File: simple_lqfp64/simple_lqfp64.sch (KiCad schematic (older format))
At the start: 47 parts, among them P1 CONN_01X02, P10 CONN_01X04, P11 CONN_01X03, P12 CONN_01X03, P13 USB_A, P14 CONN_01X01, P15 CONN_01X01, P16 CONN_01X01, P17 CONN_01X01, P18 CONN_01X01, P19 CONN_01X01, P2 CONN_01X03, P20 CONN_01X01, P21 CONN_01X01, P22 CONN_01X01, P23 CONN_01X01, P24 CONN_01X01, P25 CONN_01X01, P26 CONN_01X01, P27 CONN_01X01, P28 CONN_01X01, P29 CONN_01X01, P3 CONN_01X04, P30 CONN_01X01, P31 CONN_01X01, P32 CONN_01X01, P33 CONN_01X01, P4 CONN_01X04, P5 CONN_01X01, P6 CONN_01X04, P7 CONN_01X03, P8 CONN_01X06, P9 CONN_01X07, SW1 SW_PUSH, U1 STM32F103RCTx, U2 AP1117D33, Y1 Crystal, Y2 Crystal

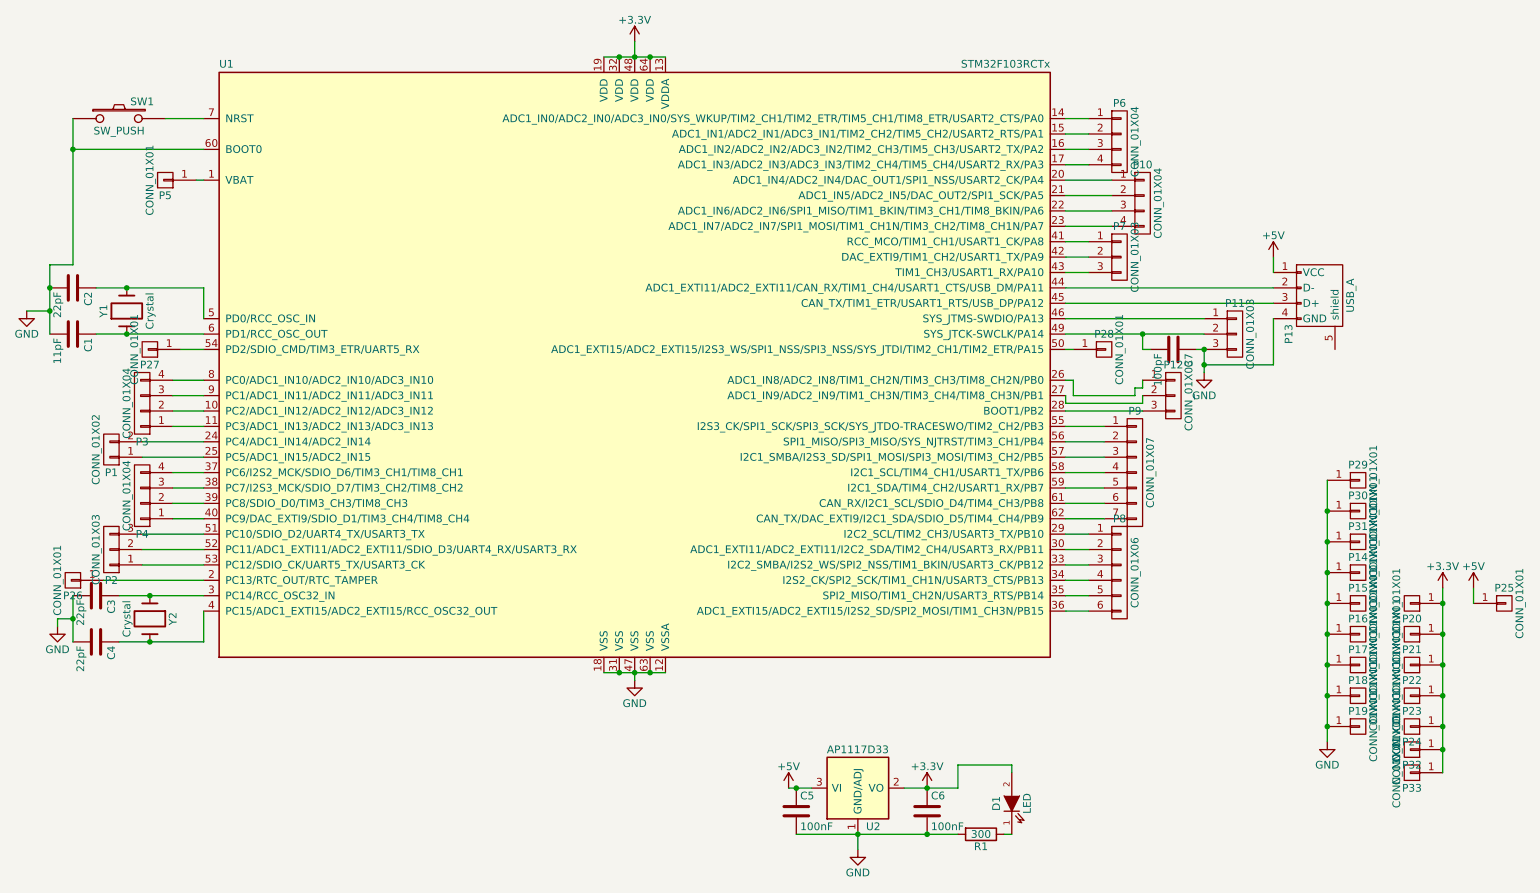
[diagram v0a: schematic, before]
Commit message: stm32 lqfp64 fixes
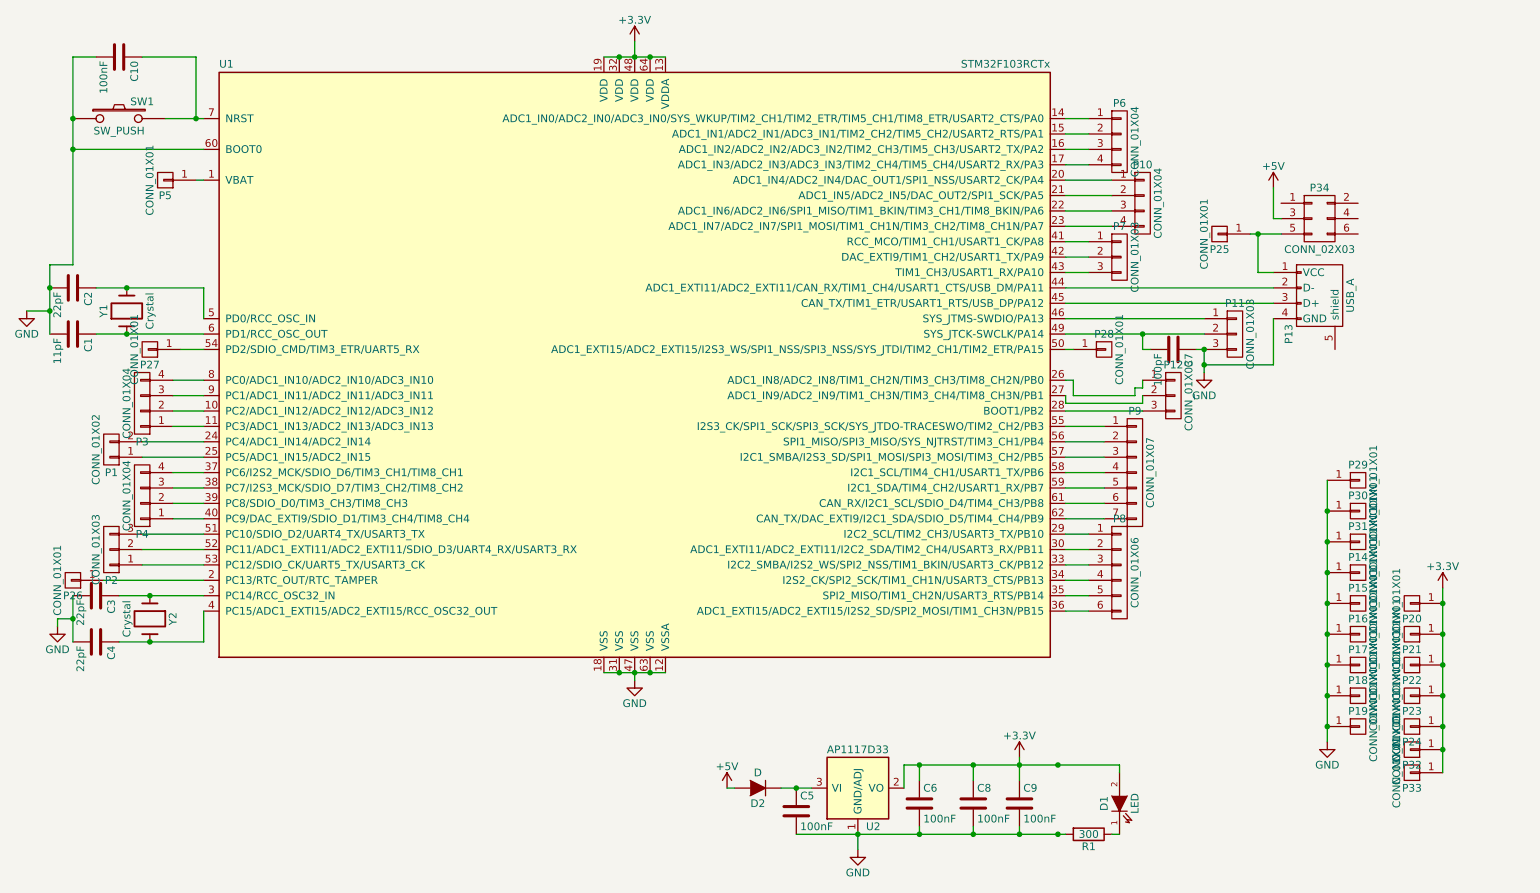
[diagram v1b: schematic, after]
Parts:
- added C10, C8, C9: 100nF, Capacitors_SMD:C_0805_HandSoldering, symbol C
- added D2: D, Diodes_ThroughHole:Diode_DO-35_SOD27_Horizontal_RM10, symbol D
- added P34: CONN_02X03, Socket_Strips:Socket_Strip_Straight_2x03, symbol CONN_02X03
- SW1: footprint Buttons_Switches_SMD:SW_SPST_B3S-1000 -> Buttons_Switches_ThroughHole:SW_PUSH_SMALL
- Y1: footprint Crystals:Crystal_HC48-U_Vertical -> Crystals:Crystal_HC49-U_Vertical
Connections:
- net +3V3: now also C8.1, C9.1
- net +5V: now also D2.2 (A), P34.3 (P3); no longer C5.1, P13.1 (VCC), P25.1 (P1), U2.3 (VI)
- net GND: now also C10.2, C8.2, C9.2
- net at SW1.2, U1.7 (NRST): now also C10.1
- new net: P13.1 (VCC), P25.1 (P1), P34.5 (P5)
- new net: C5.1, D2.1 (K), U2.3 (VI)
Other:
- moved on the sheet: C6, D1, P25, R1
